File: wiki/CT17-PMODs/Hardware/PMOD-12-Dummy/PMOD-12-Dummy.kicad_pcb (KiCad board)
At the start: 2 copper layers, 31.5 x 25.1 mm, 1 part, among them J1 Conn_02x06_Top_Bottom

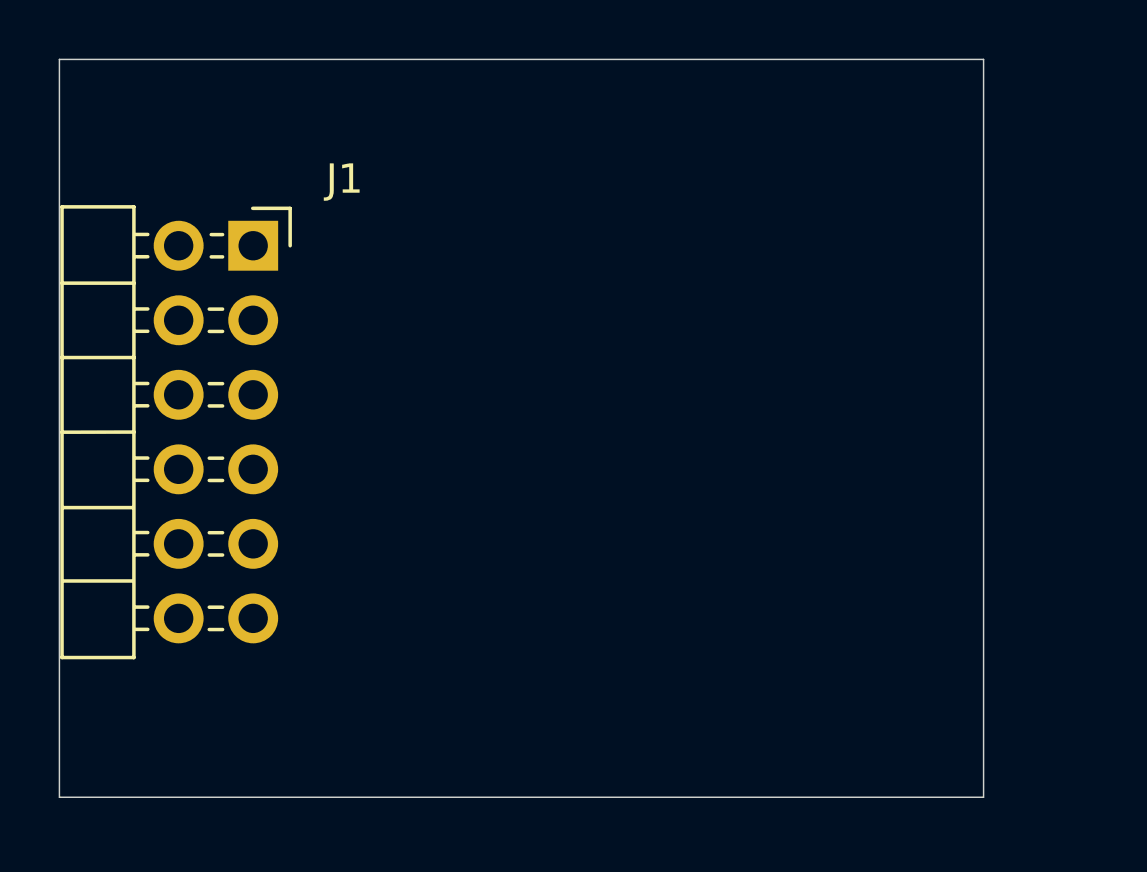
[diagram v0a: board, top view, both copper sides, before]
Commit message: CT17: update PMOD-12-Dummy kicad files
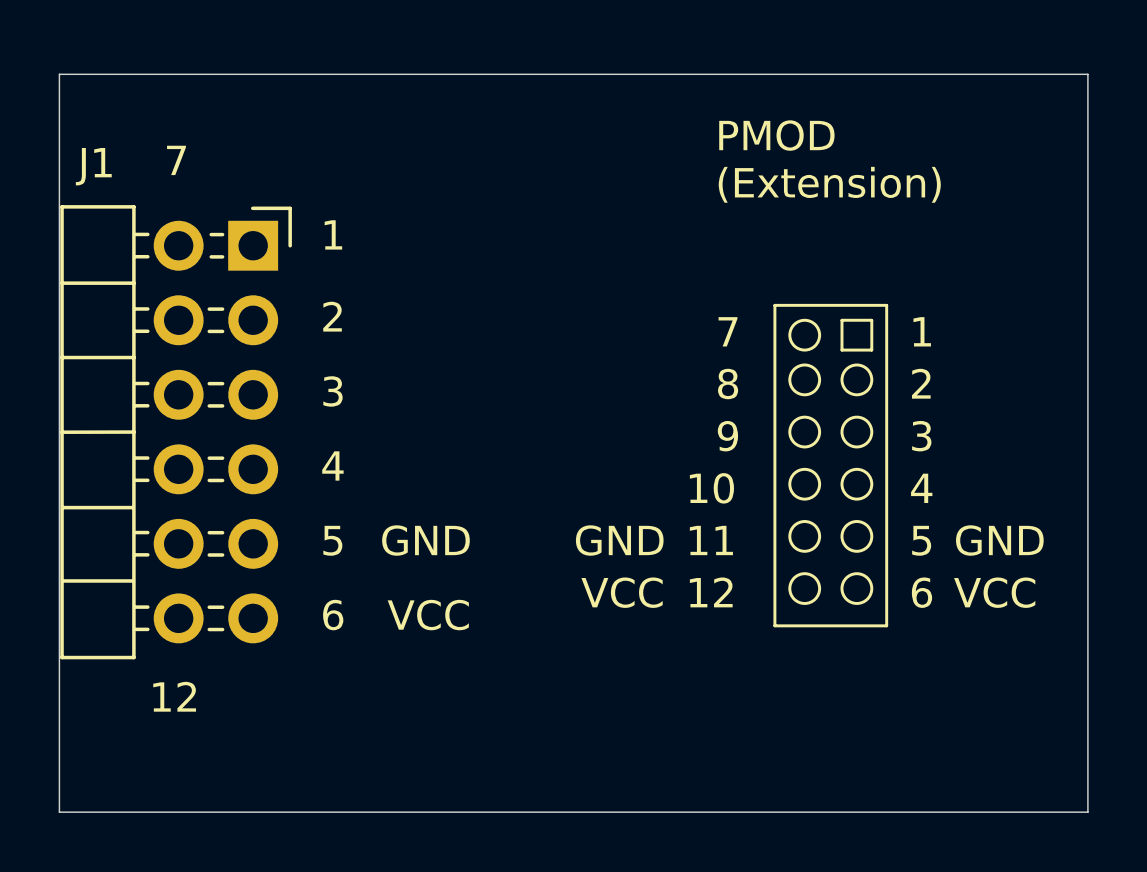
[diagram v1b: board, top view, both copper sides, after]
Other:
- board size 31.5 x 25.1 mm -> 35.1 x 25.1 mm
- board text added: "1"
- board text added: "10"
- board text added: "11"
- board text added: "12"
- board text added: "2"
- board text added: "3"
- board text added: "4"
- board text added: "5"
- board text added: "6"
- board text added: "7"
- board text added: "8"
- board text added: "9"
- board text added: "GND"
- board text added: "PMOD (Extension)"
- board text added: "VCC"
